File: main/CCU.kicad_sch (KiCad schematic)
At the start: 2 parts, among them U2 ESP32-DevKitC

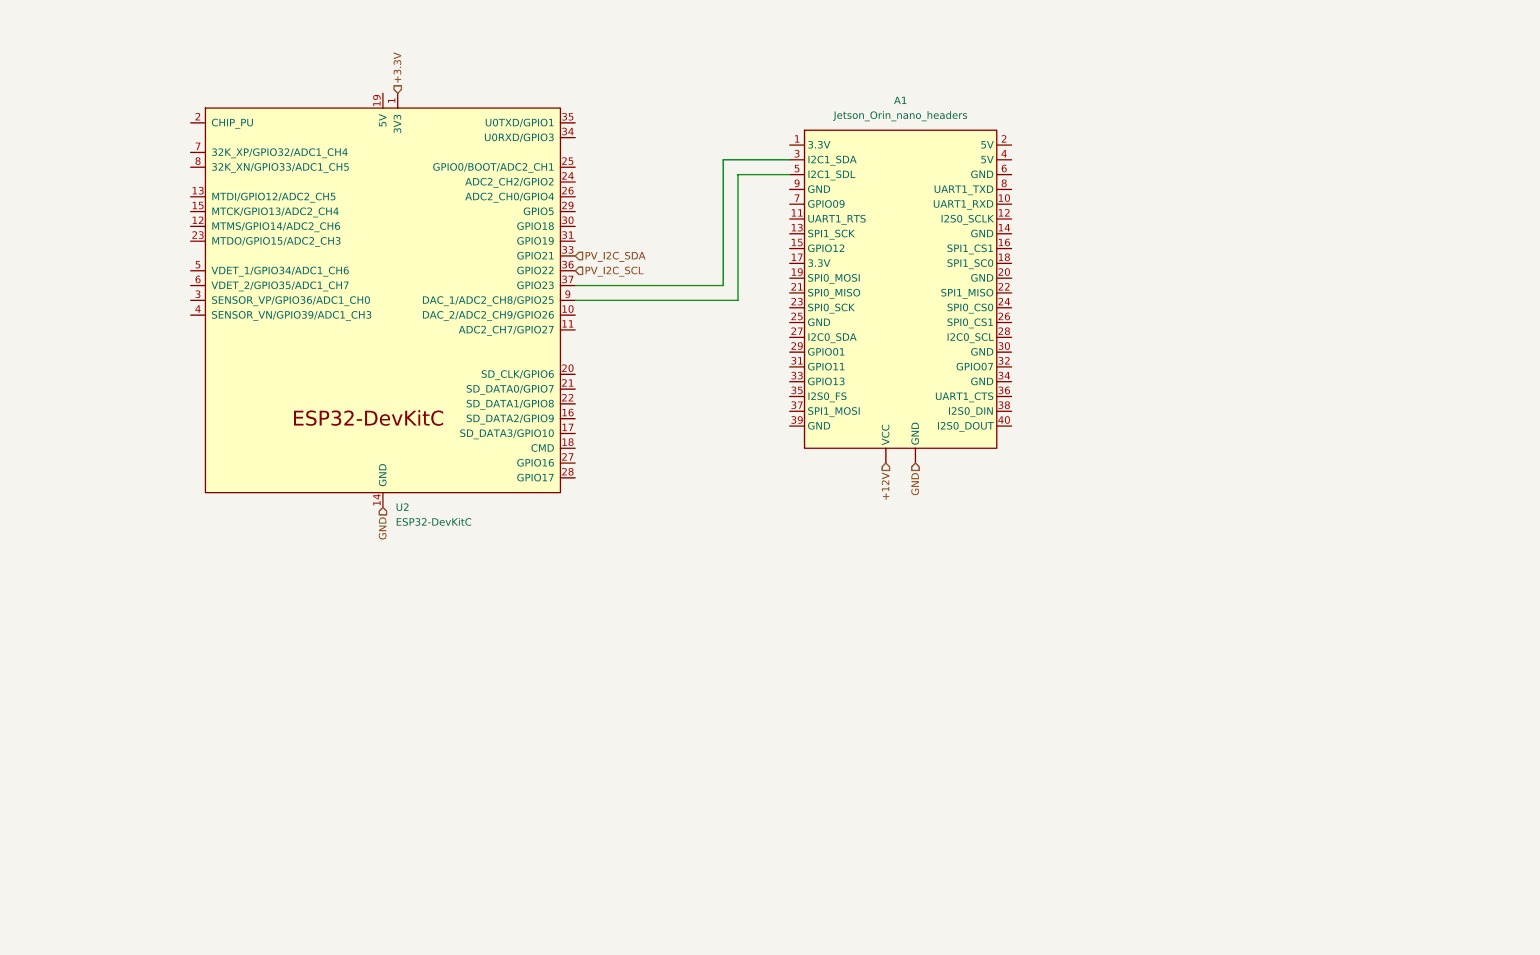
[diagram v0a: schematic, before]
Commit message: Added CAN connection from BAT to CCU(Jetson)
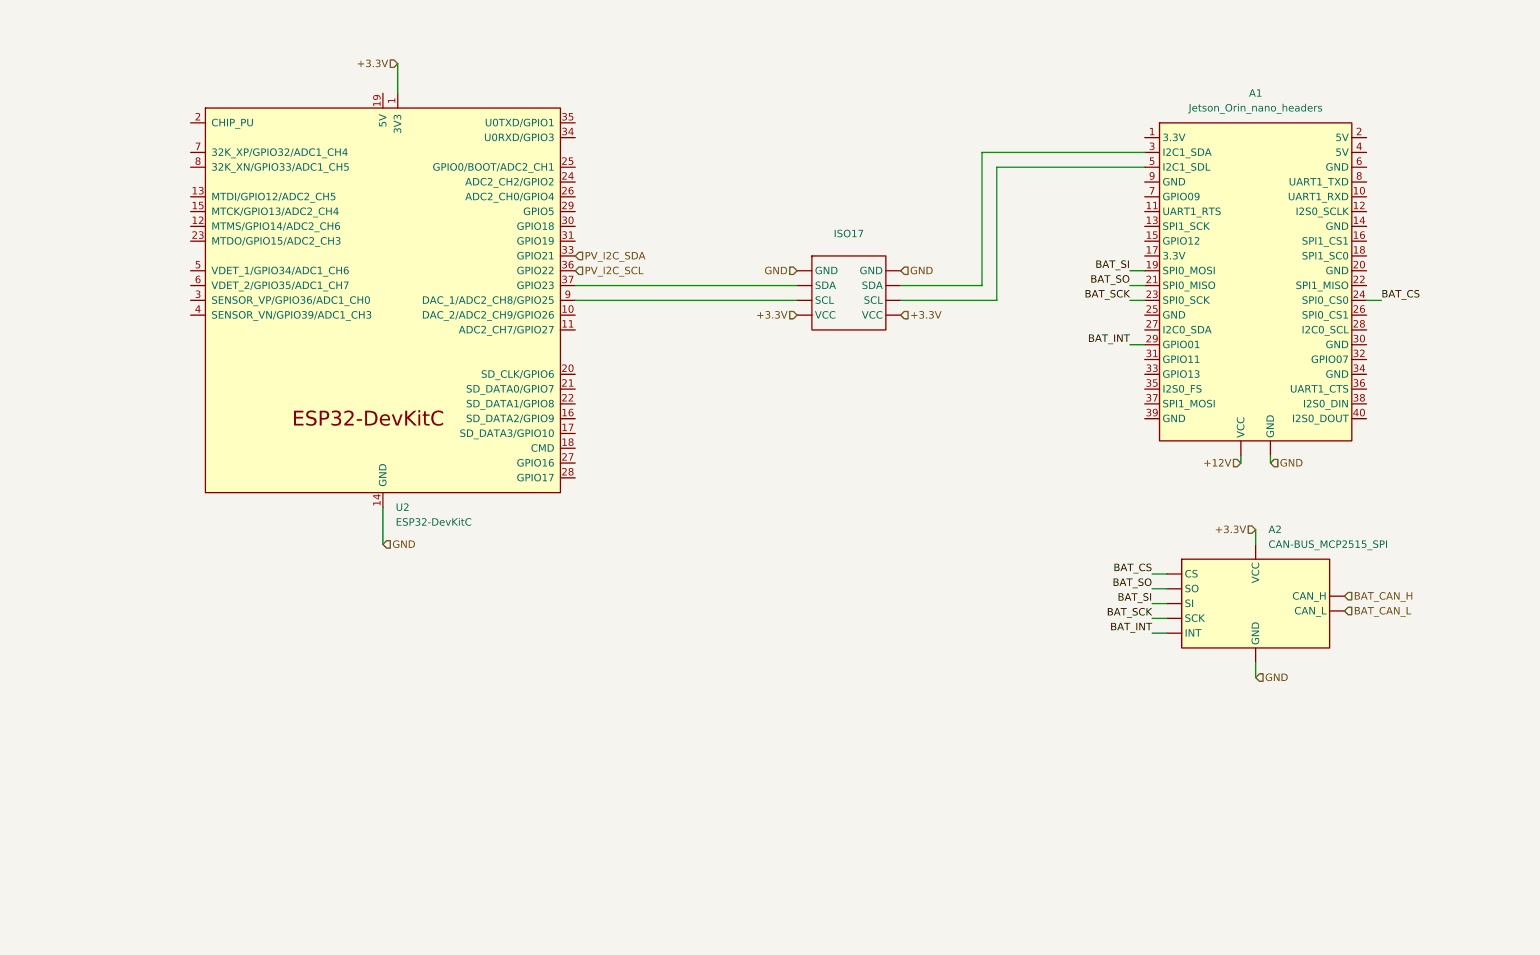
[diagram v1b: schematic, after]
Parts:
- added A2: CAN-BUS_MCP2515_SPI, symbol New_Library_0:CAN-BUS_MCP2515_SPI
- added ISO17: ~, symbol New_Library_0:Bidirectional I2C Isolator
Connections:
- net +3.3V: now also A2. (VCC), ISO17. (VCC)
- net GND: now also A2. (VCC), ISO17. (VCC)
- net at U2.37 (GPIO23): now also ISO17. (VCC); no longer A1.3 (I2C1_SDA)
- net at U2.9 (DAC_1/ADC2_CH8/GPIO25): now also ISO17. (VCC); no longer A1.5 (I2C1_SDL)
- net BAT_SI: now reaches A1.19 (SPI0_MOSI)
- net BAT_SI: now also A2. (VCC)
- net BAT_SO: now reaches A1.21 (SPI0_MISO)
- net BAT_SO: now also A2. (VCC)
- net BAT_SCK: now reaches A1.23 (SPI0_SCK)
- net BAT_SCK: now also A2. (VCC)
- net BAT_CS: now reaches A1.24 (SPI0_CS0)
- net BAT_CS: now also A2. (VCC)
- net BAT_INT: now reaches A1.29 (GPIO01)
- net BAT_INT: now also A2. (VCC)
- new net: A1.3 (I2C1_SDA), ISO17. (VCC)
- new net: A1.5 (I2C1_SDL), ISO17. (VCC)
- new net BAT_CAN_H: A2. (VCC)
- new net BAT_CAN_L: A2. (VCC)
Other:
- moved on the sheet: A1

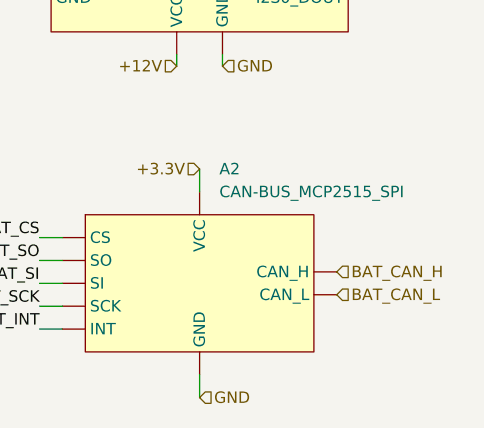
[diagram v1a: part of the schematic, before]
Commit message: Added sensors
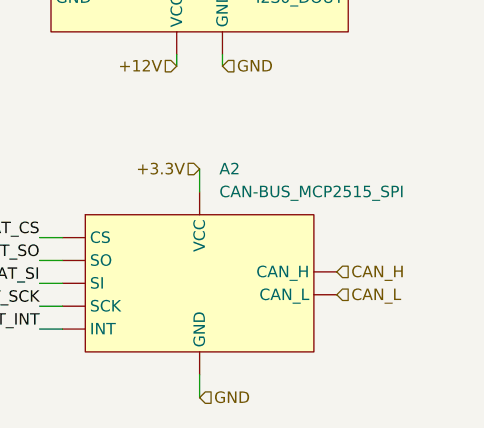
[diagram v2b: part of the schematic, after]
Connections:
- net BAT_CAN_H is gone; now on net GND: A2. (VCC)
- net BAT_CAN_L is gone; now on net GND: A2. (VCC)
- new net CAN_H: A2. (VCC)
- new net CAN_L: A2. (VCC)
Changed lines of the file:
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@@
 		)
 	)
-	(hierarchical_label "BAT_CAN_L"
+	(hierarchical_label "CAN_L"
 		(shape input)
 		(at 248.92 116.84 0)
@@
 		)
 	)
-	(hierarchical_label "BAT_CAN_H"
+	(hierarchical_label "CAN_H"
 		(shape input)
 		(at 248.92 114.3 0)

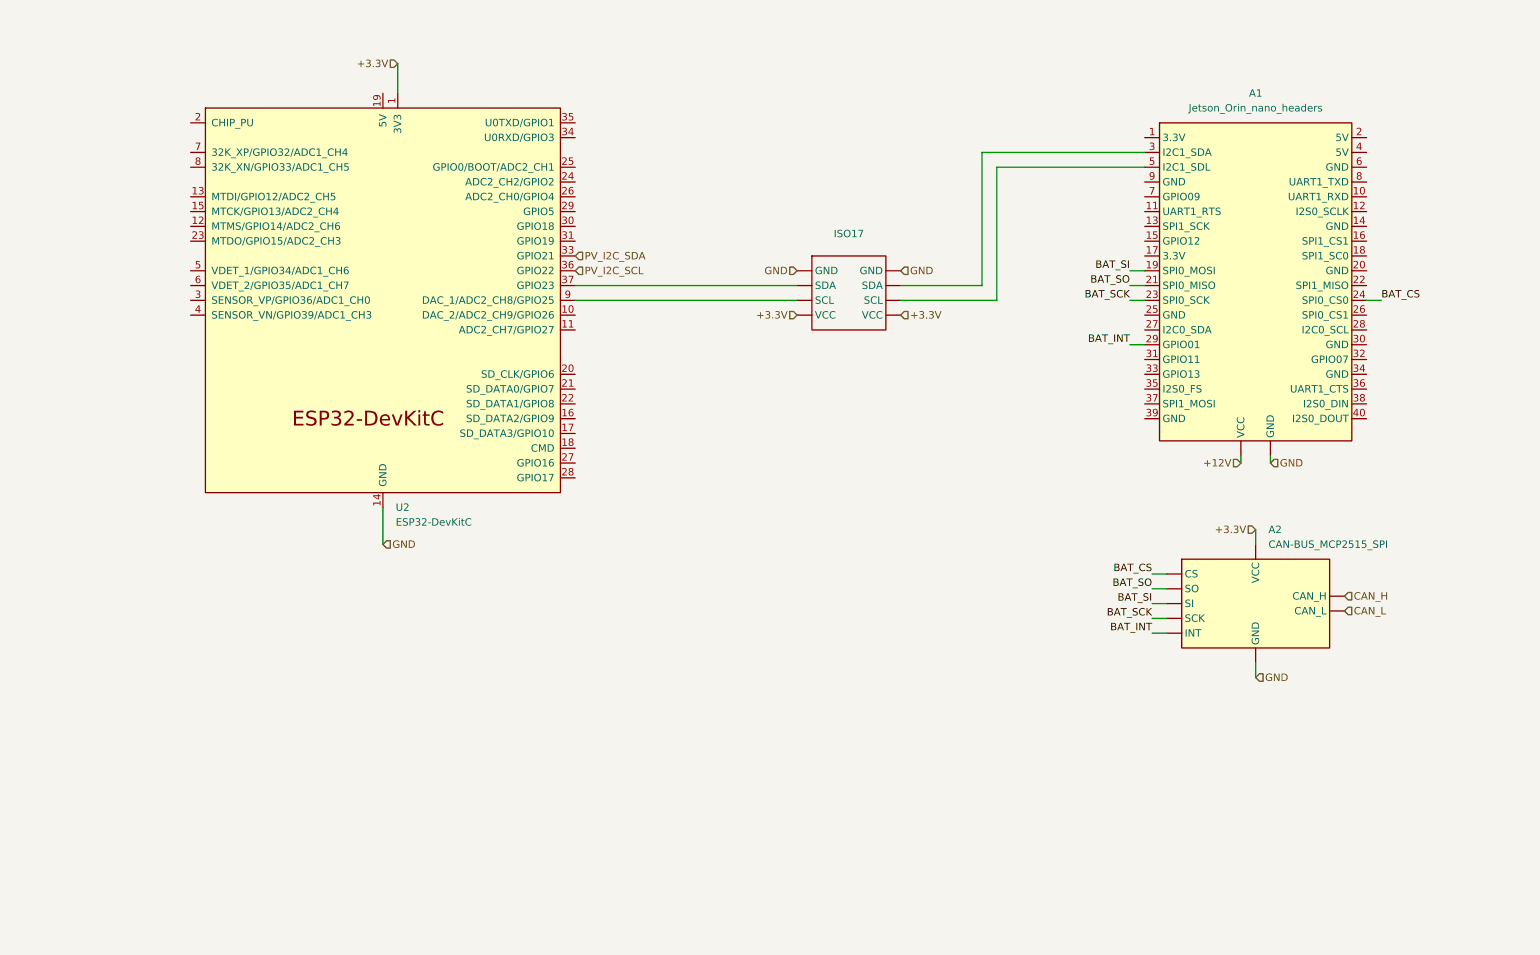
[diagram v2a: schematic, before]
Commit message: Added MPU6050 and GPS Module to CCU
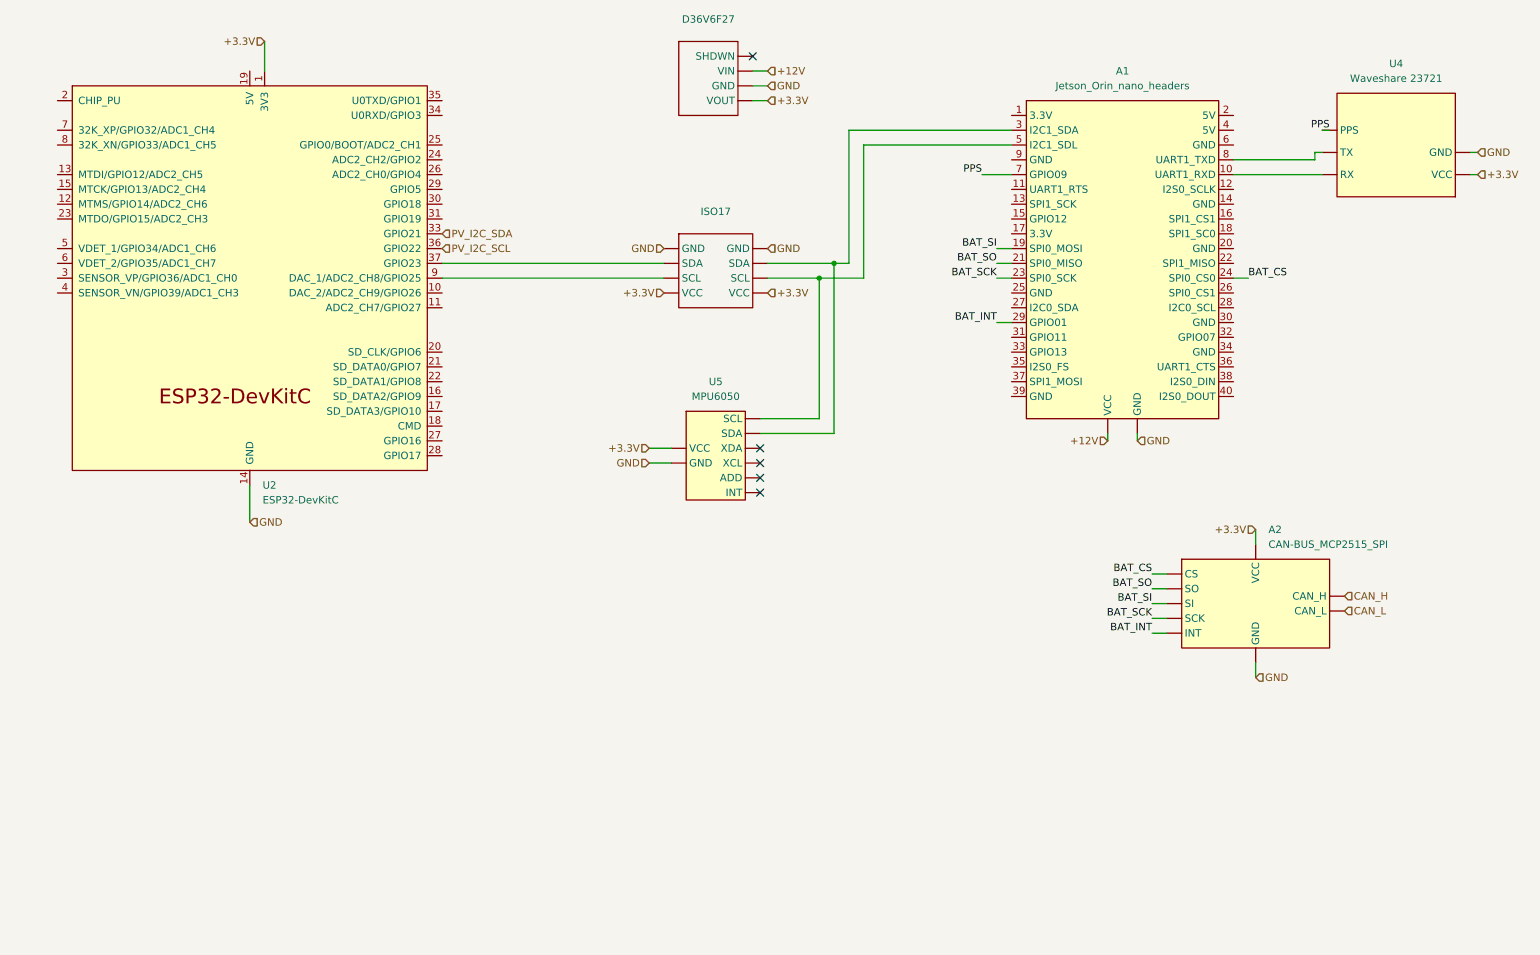
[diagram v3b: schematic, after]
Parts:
- added D36V6F27: ~, symbol New_Library_0:StepDown
- added U4: Waveshare 23721, symbol New_Library_0:Waveshare_23721
- added U5: MPU6050, symbol New_Library_0:MPU6050
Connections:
- net +12V: now also D36V6F27. (VOUT)
- net +3.3V: now also D36V6F27. (VOUT), U4. (VCC), U5. (XDA)
- net GND: now also D36V6F27. (VOUT), U4. (VCC), U5. (XDA)
- net at A1.10 (UART1_RXD): now also U4. (VCC)
- net at A1.3 (I2C1_SDA), ISO17. (VCC): now also U5. (XDA)
- net at A1.5 (I2C1_SDL), ISO17. (VCC): now also U5. (XDA)
- net PPS: now reaches A1.7 (GPIO09)
- net PPS: now also U4. (VCC)
- net at A1.8 (UART1_TXD): now also U4. (VCC)
- no-connect marks 0 -> 5
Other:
- moved on the sheet: A1, ISO17, U2

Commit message: Added new connectors to jetson Added Oak-D
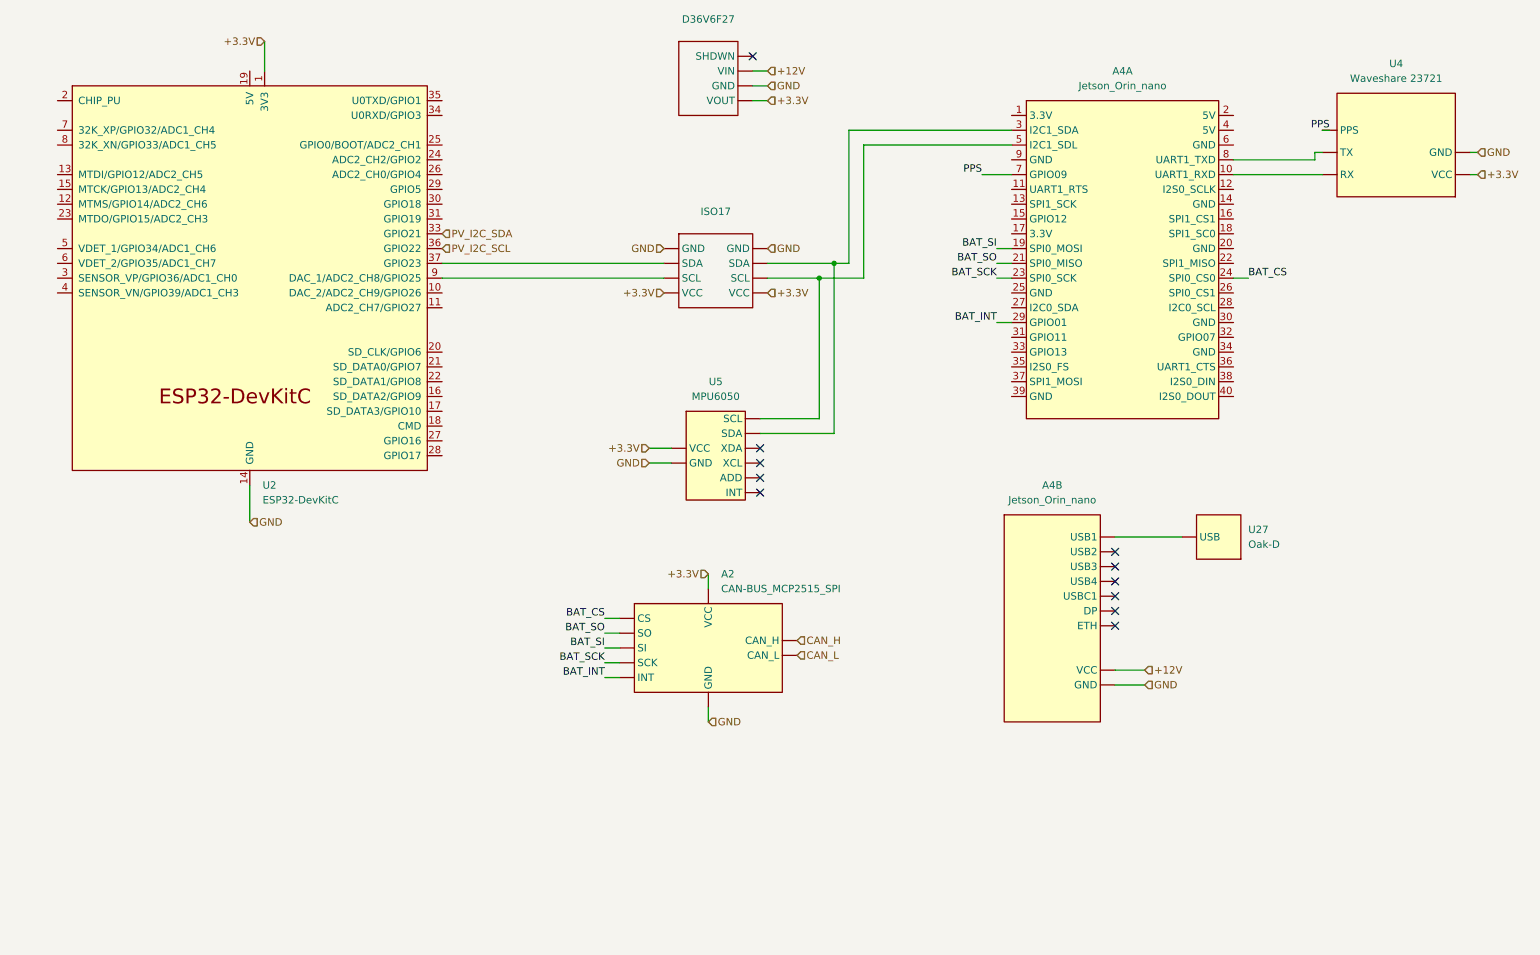
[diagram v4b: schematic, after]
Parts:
- removed A1: Jetson_Orin_nano_headers, symbol New_Library_0:Jetson_Orion_Nano
- added A4: Jetson_Orin_nano, symbol New_Library_0:Jetson_Orion_Nano
- added U27: Oak-D, symbol New_Library_0:Oak-D
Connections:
- net +12V: now also A4. (VCC)
- net BAT_CS: now also A4.24 (SPI0_CS0)
- net BAT_INT: now also A4.29 (GPIO01)
- net BAT_SCK: now also A4.23 (SPI0_SCK)
- net BAT_SI: now also A4.19 (SPI0_MOSI)
- net BAT_SO: now also A4.21 (SPI0_MISO)
- net GND: now also A4. (VCC)
- net PPS: now also A4.7 (GPIO09)
- new net: A4.3 (I2C1_SDA), ISO17. (VCC), U5. (XDA)
- new net: A4.5 (I2C1_SDL), ISO17. (VCC), U5. (XDA)
- new net: A4.10 (UART1_RXD), U4. (VCC)
- new net: A4.8 (UART1_TXD), U4. (VCC)
- new net: A4. (VCC), U27. (USB)
- no-connect marks 5 -> 11
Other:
- moved on the sheet: A2

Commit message: added sonar
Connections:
- new net: A4.3 (I2C1_SDA), ISO17. (VCC), U5. (XDA)
- new net: A4.5 (I2C1_SDL), ISO17. (VCC), U5. (XDA)
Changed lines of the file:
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@@
 	)
 	(symbol
-		(lib_name "New_Library_0:Jetson_Orion_Nano")
 		(lib_id "New_Library_0:Jetson_Orion_Nano")
 		(at 200.66 120.65 0)

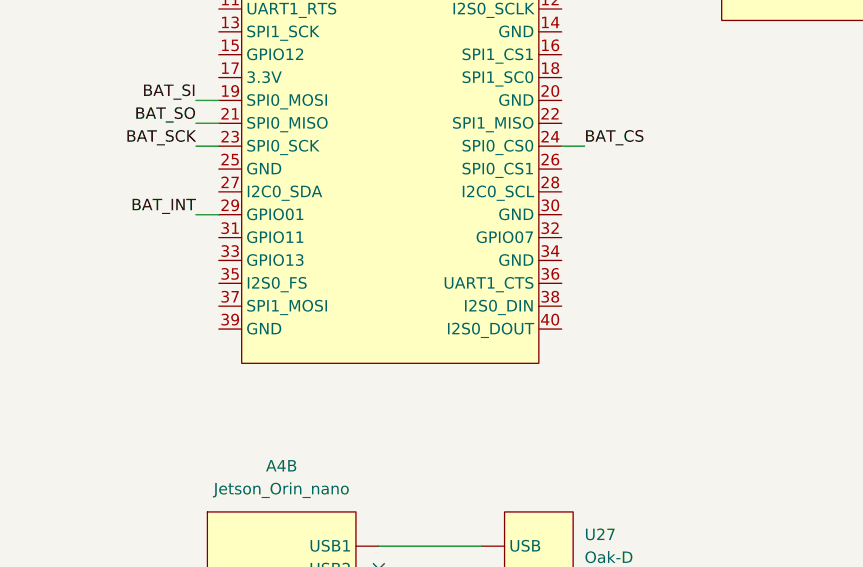
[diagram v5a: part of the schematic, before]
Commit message: Added AMS, LEDs
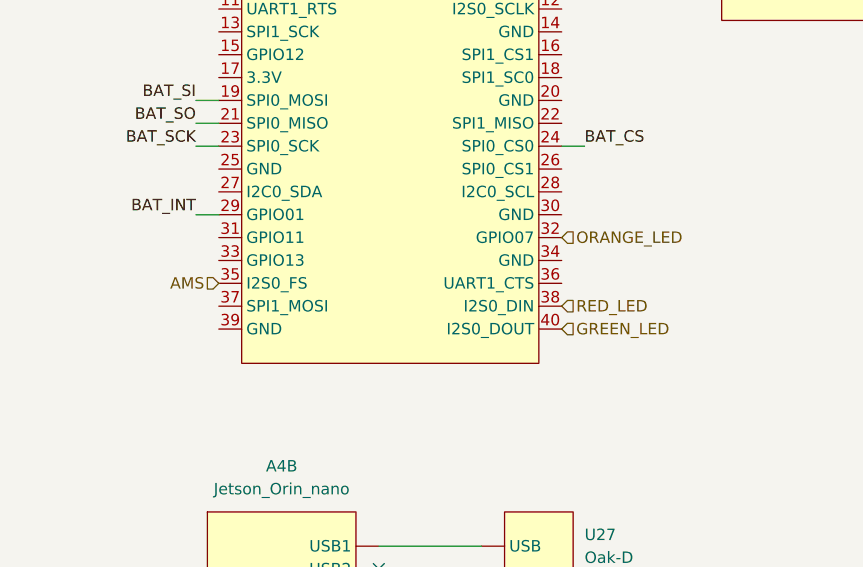
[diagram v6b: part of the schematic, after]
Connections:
- net ORANGE_LED: now reaches A4.32 (GPIO07)
- net AMS: now reaches A4.35 (I2S0_FS)
- net RED_LED: now reaches A4.38 (I2S0_DIN)
- net GREEN_LED: now reaches A4.40 (I2S0_DOUT)
- new net: A4.3 (I2C1_SDA), ISO17. (VCC), U5. (XDA)
- new net: A4.5 (I2C1_SDL), ISO17. (VCC), U5. (XDA)
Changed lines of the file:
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@@
+		)
+	)
+	(hierarchical_label "RED_LED"
+		(shape input)
+		(at 229.87 77.47 0)
+		(fields_autoplaced yes)
+		(effects
+			(font
+				(size 1.27 1.27)
+			)
+			(justify left)
 		)
 	)
@@
 		)
 	)
+	(hierarchical_label "GREEN_LED"
+		(shape input)
+		(at 229.87 80.01 0)
+		(fields_autoplaced yes)
+		(effects
+			(font
+				(size 1.27 1.27)
+			)
+			(justify left)
+		)
+	)
 	(hierarchical_label "GND"
 		(shape input)
@@
 		)
 	)
+	(hierarchical_label "ORANGE_LED"
+		(shape input)
+		(at 229.87 69.85 0)
+		(fields_autoplaced yes)
+		(effects
+			(font
+				(size 1.27 1.27)
+			)
+			(justify left)
+		)
+	)
 	(hierarchical_label "+3.3V"
 		(shape input)
@@
 		(fields_autoplaced yes)
 		(effects
+			(font
+				(size 1.27 1.27)
+			)
+			(justify right)
+		)
+	)
+	(hierarchical_label "AMS"
+		(shape input)
+		(at 191.77 74.93 180)
+		(fields_autoplaced yes)
+		(effects
